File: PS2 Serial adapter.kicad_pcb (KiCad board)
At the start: 2 copper layers, 34 x 18 mm, 11 parts, among them J1 PS2, J2 PC, U1 MAX3323EEUE

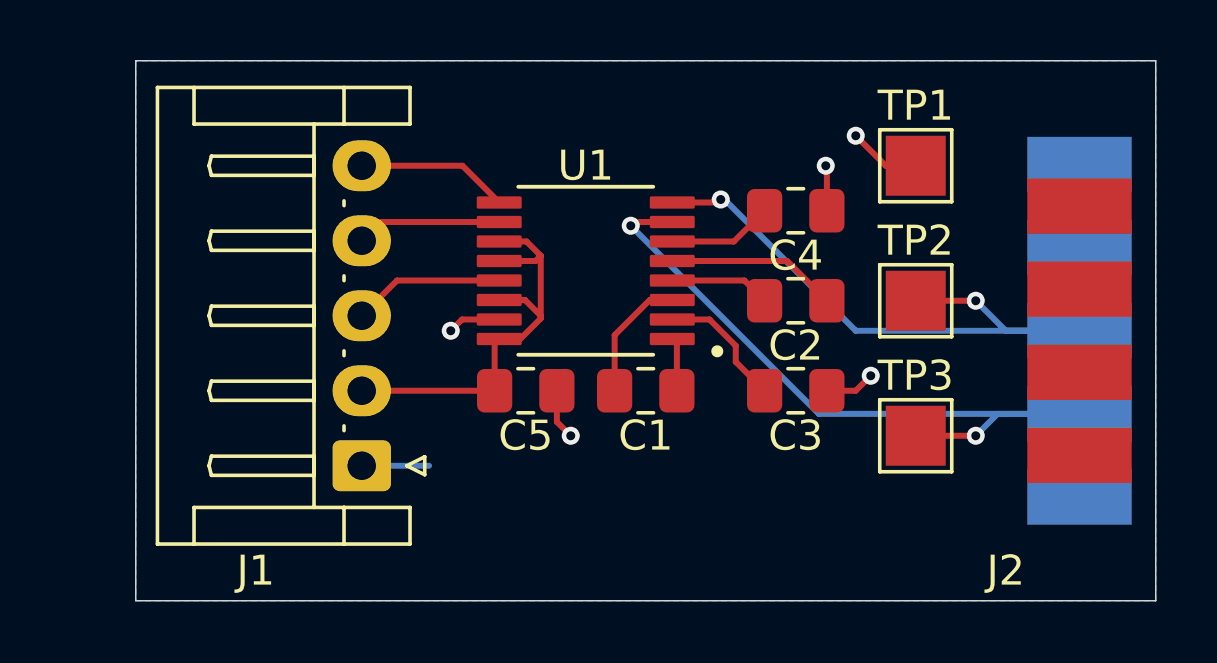
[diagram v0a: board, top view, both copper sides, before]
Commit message: Update footprints, 3V3 width and begin bom
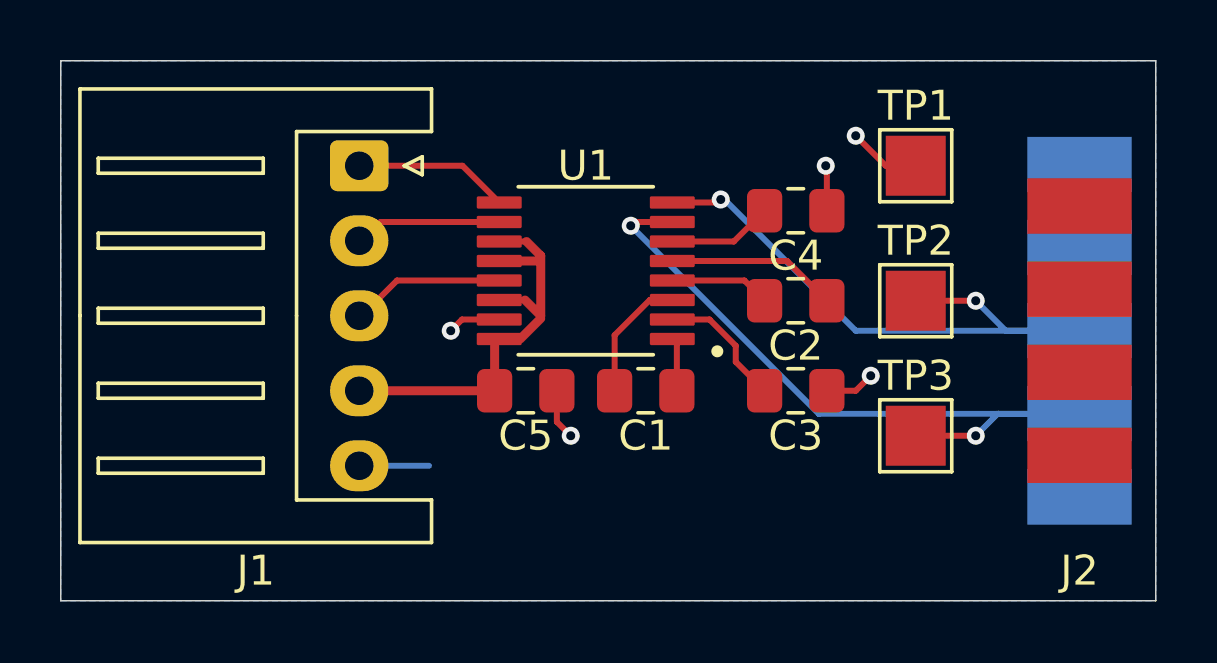
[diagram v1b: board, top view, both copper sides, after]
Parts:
- J1: footprint Connector_JST:JST_EH_S5B-EH_1x05_P2.50mm_Horizontal -> Connector_JST:JST_XH_S5B-XH-A_1x05_P2.50mm_Horizontal
- moved J1 10.0 mm to (127.5, 54.5), turned to -90 degrees
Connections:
- J1 pad 1: GND -> /EE_RXD
- J1 pad 2: +3.3V -> /EE_TXD
- J1 pad 4: /EE_TXD -> +3.3V
- J1 pad 5: /EE_RXD -> GND
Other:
- board size 34 x 18 mm -> 36.5 x 18 mm
